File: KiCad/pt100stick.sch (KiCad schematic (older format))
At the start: 9 parts, among them U1 MAX31865ATP_

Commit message: Start Project Lib / Relayout
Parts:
- A1: symbol Driver_Motor:Pololu_Breakout_A4988 -> PT100stick:Pololu_Breakout_A4988
- C1, C2: symbol Device:C_Small -> PT100stick:C_Small
- FB1: symbol Device:Ferrite_Bead_Small -> PT100stick:Ferrite_Bead_Small
- JP1, JP2: footprint Jumper:SolderJumper-2_P1.3mm_Open_TrianglePad1.0x1.5mm -> Jumper:SolderJumper-2_P1.3mm_Bridged_Pad1.0x1.5mm; symbol Jumper:SolderJumper_2_Bridged -> PT100stick:SolderJumper_2_Bridged
- R1: symbol Device:R_Small_US -> PT100stick:R_Small_US
- U1: symbol dk_PMIC-Thermal-Management:MAX31865ATP_ -> PT100stick:MAX31865ATP_
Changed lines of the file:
@@
 $EndDescr
 $Comp
-L Driver_Motor:Pololu_Breakout_A4988 A1
+L PT100stick:Pololu_Breakout_A4988 A1
 U 1 1 5EB9E565
 P 1900 2050
@@
 SCK
 $Comp
-L power:GND #PWR0101
+L PT100stick:GND #PWR0101
 U 1 1 5EBA0B0B
 P 2000 2950
@@
 	2000 2900 2100 2900
 $Comp
-L power:+3.3V #PWR0102
+L PT100stick:+3.3V #PWR0102
 U 1 1 5EBA1652
 P 1900 1100
@@
 	1900 1100 1900 1350
 $Comp
-L dk_PMIC-Thermal-Management:MAX31865ATP_ U1
+L PT100stick:MAX31865ATP_ U1
 U 1 1 5EBA27E8
 P 5150 1700
@@
 	4450 2500 4650 2500
 $Comp
-L power:GND #PWR0104
+L PT100stick:GND #PWR0104
 U 1 1 5EBA5AB3
 P 5200 2900
@@
 Wire Wire Line
 	5200 2850 5250 2850
-$Comp
-L power:+3.3V #PWR0105
-U 1 1 5EBA7D45
-P 5200 900
-F 0 "#PWR0105" H 5200 750 50  0001 C CNN
-F 1 "+3.3V" H 5215 1073 50  0000 C CNN
-F 2 "" H 5200 900 50  0001 C CNN
-F 3 "" H 5200 900 50  0001 C CNN
-	1    5200 900
-	1    0    0    -1
-$EndComp
 Wire Wire Line
 	5200 900  5200 950
@@
 	4600 1800 4650 1800
 $Comp
-L Device:R_Small_US R1
+L PT100stick:R_Small_US R1
 U 1 1 5EBADD3B
 P 4250 1700
@@
 FORCE+
 $Comp
-L Device:C_Small C1
+L PT100stick:C_Small C1
 U 1 1 5EBB292B
 P 2950 2100
@@
 $EndComp
 $Comp
-L Jumper:SolderJumper_2_Bridged JP1
+L PT100stick:SolderJumper_2_Bridged JP1
 U 1 1 5EBAE765
 P 2650 2250
 F 0 "JP1" H 2650 2025 50  0000 C CNN
 F 1 "Cut for 4" H 2650 2116 50  0000 C CNN
-F 2 "Jumper:SolderJumper-2_P1.3mm_Open_TrianglePad1.0x1.5mm" H 2650 2250 50  0001 C CNN
+F 2 "Jumper:SolderJumper-2_P1.3mm_Bridged_Pad1.0x1.5mm" H 2650 2250 50  0001 C CNN
 F 3 "~" H 2650 2250 50  0001 C CNN
 	1    2650 2250
@@
 $EndComp
 $Comp
-L Jumper:SolderJumper_2_Bridged JP2
+L PT100stick:SolderJumper_2_Bridged JP2
 U 1 1 5EBB06B7
 P 2650 1950
 F 0 "JP2" H 2650 2155 50  0000 C CNN
 F 1 "Cut for 3/4" H 2650 2064 50  0000 C CNN
-F 2 "Jumper:SolderJumper-2_P1.3mm_Open_TrianglePad1.0x1.5mm" H 2650 1950 50  0001 C CNN
+F 2 "Jumper:SolderJumper-2_P1.3mm_Bridged_Pad1.0x1.5mm" H 2650 1950 50  0001 C CNN
 F 3 "~" H 2650 1950 50  0001 C CNN
 	1    2650 1950
@@
 FORCE-
 $Comp
-L Device:C_Small C2
+L PT100stick:C_Small C2
 U 1 1 5EC2A459
-P 6000 1050
-F 0 "C2" H 6092 1096 50  0000 L CNN
-F 1 "0.1uF" H 6092 1005 50  0000 L CNN
-F 2 "Capacitor_SMD:C_0603_1608Metric_Pad1.05x0.95mm_HandSolder" H 6000 1050 50  0001 C CNN
-F 3 "~" H 6000 1050 50  0001 C CNN
-	1    6000 1050
-	1    0    0    -1
-$EndComp
-$Comp
-L power:+3.3V #PWR0103
-U 1 1 5EC2B8B9
-P 6000 900
-F 0 "#PWR0103" H 6000 750 50  0001 C CNN
-F 1 "+3.3V" H 6015 1073 50  0000 C CNN
-F 2 "" H 6000 900 50  0001 C CNN
-F 3 "" H 6000 900 50  0001 C CNN
-	1    6000 900
-	1    0    0    -1
-$EndComp
-Wire Wire Line
-	6000 900  6000 950
-$Comp
-L power:GND #PWR0107
-U 1 1 5EC2E090
-P 6000 1200
-F 0 "#PWR0107" H 6000 950 50  0001 C CNN
-F 1 "GND" H 6005 1027 50  0000 C CNN
-F 2 "" H 6000 1200 50  0001 C CNN
-F 3 "" H 6000 1200 50  0001 C CNN
-	1    6000 1200
-	1    0    0    -1
-$EndComp
-Wire Wire Line
-	6000 1150 6000 1200
-$Comp
-L Device:Ferrite_Bead_Small FB1
+P 6250 1650
+F 0 "C2" H 6342 1696 50  0000 L CNN
+F 1 "0.1uF" H 6342 1605 50  0000 L CNN
+F 2 "Capacitor_SMD:C_0603_1608Metric_Pad1.05x0.95mm_HandSolder" H 6250 1650 50  0001 C CNN
+F 3 "~" H 6250 1650 50  0001 C CNN
+	1    6250 1650
+	1    0    0    -1
+$EndComp
+Wire Wire Line
+	6250 1500 6250 1550
+Wire Wire Line
+	6250 1750 6250 1800
+$Comp
+L PT100stick:Ferrite_Bead_Small FB1
 U 1 1 5EC32E91
 P 5250 1150
@@
 Wire Wire Line
 	5250 1400 5250 1250
+$Comp
+L PT100stick:+3.3V #PWR?
+U 1 1 5EBCE55F
+P 5200 900
+F 0 "#PWR?" H 5200 750 50  0001 C CNN
+F 1 "+3.3V" H 5215 1073 50  0000 C CNN
+F 2 "" H 5200 900 50  0001 C CNN
+F 3 "" H 5200 900 50  0001 C CNN
+	1    5200 900
+	1    0    0    -1
+$EndComp
+$Comp
+L PT100stick:+3.3V #PWR?
+U 1 1 5EBD5DBE
+P 6250 1500
+F 0 "#PWR?" H 6250 1350 50  0001 C CNN
+F 1 "+3.3V" H 6265 1673 50  0000 C CNN
+F 2 "" H 6250 1500 50  0001 C CNN
+F 3 "" H 6250 1500 50  0001 C CNN
+	1    6250 1500
+	1    0    0    -1
+$EndComp
+$Comp
+L PT100stick:GND #PWR?
+U 1 1 5EBD76AE
+P 6250 1800
+F 0 "#PWR?" H 6250 1550 50  0001 C CNN
+F 1 "GND" H 6255 1627 50  0000 C CNN
+F 2 "" H 6250 1800 50  0001 C CNN
+F 3 "" H 6250 1800 50  0001 C CNN
+	1    6250 1800
+	1    0    0    -1
+$EndComp
 $EndSCHEMATC

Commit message: Moved all footprints to project lib (I think)
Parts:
- A1: footprint Module:Pololu_Breakout-16_15.2x20.3mm -> PT100Stick:Pololu_Breakout-16_15.2x20.3mm
- C1, C2: footprint Capacitor_SMD:C_0603_1608Metric_Pad1.05x0.95mm_HandSolder -> PT100Stick:C_0603_1608Metric_Pad1.05x0.95mm_HandSolder
- FB1: footprint Inductor_SMD:L_0603_1608Metric_Pad1.05x0.95mm_HandSolder -> PT100Stick:L_0603_1608Metric_Pad1.05x0.95mm_HandSolder
- JP1, JP2: footprint Jumper:SolderJumper-2_P1.3mm_Bridged_Pad1.0x1.5mm -> PT100Stick:SolderJumper-2_P1.3mm_Bridged_Pad1.0x1.5mm
- JP3: footprint Jumper:SolderJumper-3_P1.3mm_Bridged12_Pad1.0x1.5mm -> PT100Stick:SolderJumper-3_P1.3mm_Bridged12_Pad1.0x1.5mm
- R1: footprint Resistor_SMD:R_0603_1608Metric_Pad1.05x0.95mm_HandSolder -> PT100Stick:R_0603_1608Metric_Pad1.05x0.95mm_HandSolder
- U1: footprint digikey-footprints:TQFN-20-1EP_5x5mm -> PT100Stick:TQFN-20-1EP_5x5mm_P0.65mm_EP3.1x3.1mm
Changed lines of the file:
@@
 F 0 "A1" H 1950 2931 50  0000 C CNN
 F 1 "Pololu_Breakout_A4988" H 1950 2840 50  0000 C CNN
-F 2 "Module:Pololu_Breakout-16_15.2x20.3mm" H 2175 1300 50  0001 L CNN
+F 2 "PT100Stick:Pololu_Breakout-16_15.2x20.3mm" H 2175 1300 50  0001 L CNN
 F 3 "https://www.pololu.com/product/2980/pictures" H 2000 1750 50  0001 C CNN
 	1    1900 2050
@@
 F 0 "U1" H 4800 2200 60  0000 C CNN
 F 1 "MAX31865ATP_" H 4800 2100 60  0000 C CNN
-F 2 "digikey-footprints:TQFN-20-1EP_5x5mm" H 5350 1900 60  0001 L CNN
+F 2 "PT100Stick:TQFN-20-1EP_5x5mm_P0.65mm_EP3.1x3.1mm" H 5350 1900 60  0001 L CNN
 F 3 "https://datasheets.maximintegrated.com/en/ds/MAX31865.pdf" H 5350 2000 60  0001 L CNN
 F 4 "MAX31865ATP+-ND" H 5350 2100 60  0001 L CNN "Digi-Key_PN"
@@
 F 0 "R1" H 4183 1654 50  0000 R CNN
 F 1 "430" H 4183 1745 50  0000 R CNN
-F 2 "Resistor_SMD:R_0603_1608Metric_Pad1.05x0.95mm_HandSolder" H 4250 1700 50  0001 C CNN
+F 2 "PT100Stick:R_0603_1608Metric_Pad1.05x0.95mm_HandSolder" H 4250 1700 50  0001 C CNN
 F 3 "~" H 4250 1700 50  0001 C CNN
 	1    4250 1700
@@
 F 0 "C1" H 3042 2146 50  0000 L CNN
 F 1 "0.1uF" H 3042 2055 50  0000 L CNN
-F 2 "Capacitor_SMD:C_0603_1608Metric_Pad1.05x0.95mm_HandSolder" H 2950 2100 50  0001 C CNN
+F 2 "PT100Stick:C_0603_1608Metric_Pad1.05x0.95mm_HandSolder" H 2950 2100 50  0001 C CNN
 F 3 "~" H 2950 2100 50  0001 C CNN
 	1    2950 2100
@@
 F 0 "JP1" H 2650 2025 50  0000 C CNN
 F 1 "Cut for 4" H 2650 2116 50  0000 C CNN
-F 2 "Jumper:SolderJumper-2_P1.3mm_Bridged_Pad1.0x1.5mm" H 2650 2250 50  0001 C CNN
+F 2 "PT100Stick:SolderJumper-2_P1.3mm_Bridged_Pad1.0x1.5mm" H 2650 2250 50  0001 C CNN
 F 3 "~" H 2650 2250 50  0001 C CNN
 	1    2650 2250
@@
 F 0 "JP2" H 2650 2155 50  0000 C CNN
 F 1 "Cut for 3/4" H 2650 2064 50  0000 C CNN
-F 2 "Jumper:SolderJumper-2_P1.3mm_Bridged_Pad1.0x1.5mm" H 2650 1950 50  0001 C CNN
+F 2 "PT100Stick:SolderJumper-2_P1.3mm_Bridged_Pad1.0x1.5mm" H 2650 1950 50  0001 C CNN
 F 3 "~" H 2650 1950 50  0001 C CNN
 	1    2650 1950
@@
 F 0 "JP3" V 3300 1950 50  0000 L CNN
 F 1 "SolderJumper_3_Bridged12" V 2750 1700 50  0000 L CNN
-F 2 "Jumper:SolderJumper-3_P1.3mm_Bridged12_Pad1.0x1.5mm" H 3400 2200 50  0001 C CNN
+F 2 "PT100Stick:SolderJumper-3_P1.3mm_Bridged12_Pad1.0x1.5mm" H 3400 2200 50  0001 C CNN
 F 3 "~" H 3400 2200 50  0001 C CNN
 	1    3400 2200
@@
 F 0 "C2" H 6342 1696 50  0000 L CNN
 F 1 "0.1uF" H 6342 1605 50  0000 L CNN
-F 2 "Capacitor_SMD:C_0603_1608Metric_Pad1.05x0.95mm_HandSolder" H 6250 1650 50  0001 C CNN
+F 2 "PT100Stick:C_0603_1608Metric_Pad1.05x0.95mm_HandSolder" H 6250 1650 50  0001 C CNN
 F 3 "~" H 6250 1650 50  0001 C CNN
 	1    6250 1650
@@
 F 0 "FB1" H 5350 1196 50  0000 L CNN
 F 1 "Ferrite_Bead_Small" H 5350 1105 50  0000 L CNN
-F 2 "Inductor_SMD:L_0603_1608Metric_Pad1.05x0.95mm_HandSolder" V 5180 1150 50  0001 C CNN
+F 2 "PT100Stick:L_0603_1608Metric_Pad1.05x0.95mm_HandSolder" V 5180 1150 50  0001 C CNN
 F 3 "~" H 5250 1150 50  0001 C CNN
 	1    5250 1150
@@
 	5250 1400 5250 1250
 $Comp
-L PT100stick:+3.3V #PWR?
+L PT100stick:+3.3V #PWR0103
 U 1 1 5EBCE55F
 P 5200 900
-F 0 "#PWR?" H 5200 750 50  0001 C CNN
+F 0 "#PWR0103" H 5200 750 50  0001 C CNN
 F 1 "+3.3V" H 5215 1073 50  0000 C CNN
 F 2 "" H 5200 900 50  0001 C CNN
@@
 $EndComp
 $Comp
-L PT100stick:+3.3V #PWR?
+L PT100stick:+3.3V #PWR0105
 U 1 1 5EBD5DBE
 P 6250 1500
-F 0 "#PWR?" H 6250 1350 50  0001 C CNN
+F 0 "#PWR0105" H 6250 1350 50  0001 C CNN
 F 1 "+3.3V" H 6265 1673 50  0000 C CNN
 F 2 "" H 6250 1500 50  0001 C CNN
@@
 $EndComp
 $Comp
-L PT100stick:GND #PWR?
+L PT100stick:GND #PWR0107
 U 1 1 5EBD76AE
 P 6250 1800
-F 0 "#PWR?" H 6250 1550 50  0001 C CNN
+F 0 "#PWR0107" H 6250 1550 50  0001 C CNN
 F 1 "GND" H 6255 1627 50  0000 C CNN
 F 2 "" H 6250 1800 50  0001 C CNN

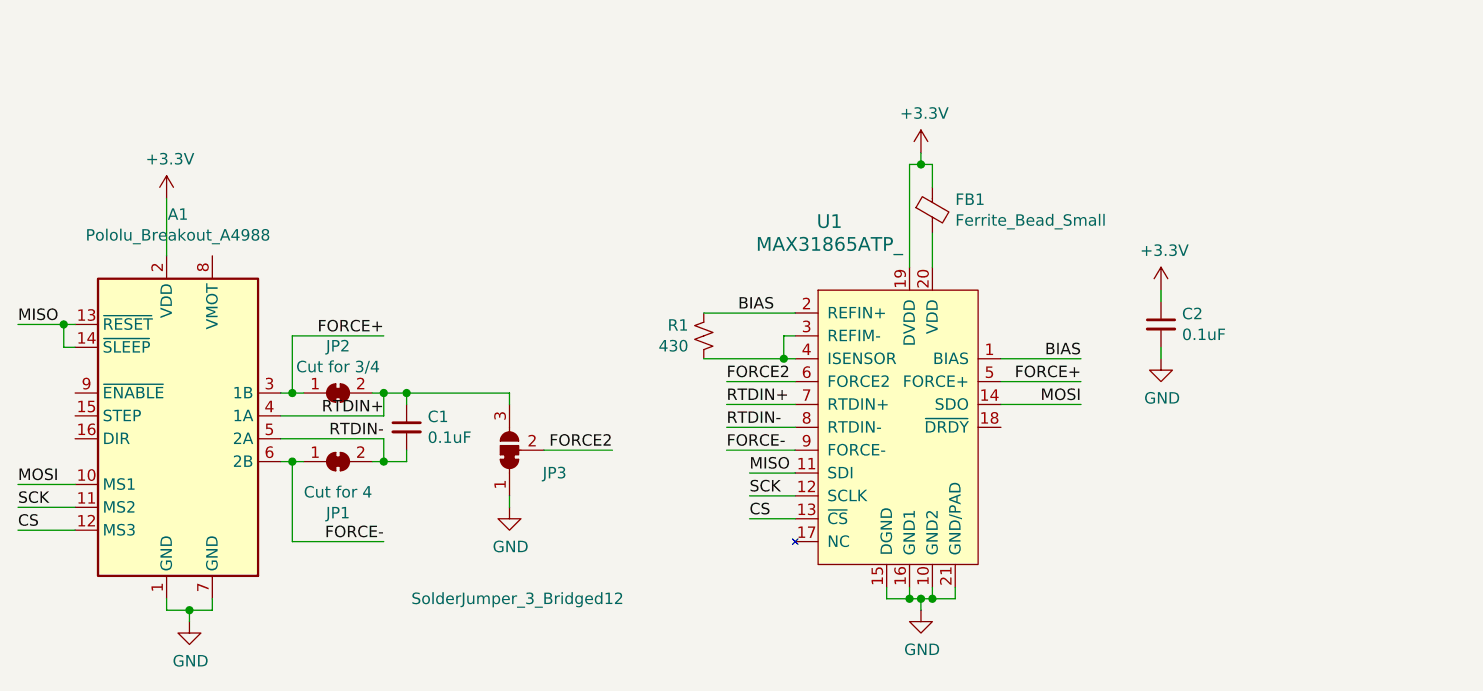
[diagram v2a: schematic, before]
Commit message: Reworked layout
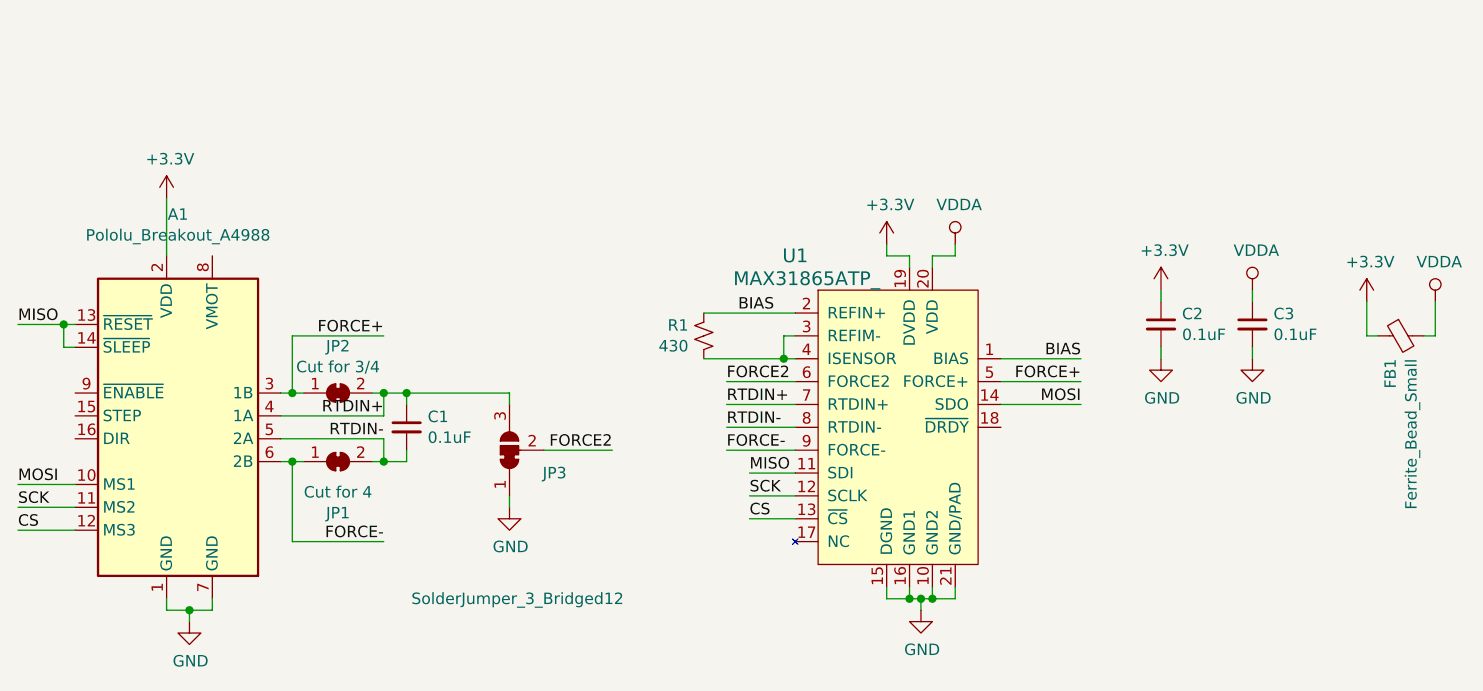
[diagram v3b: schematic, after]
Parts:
- added C3: 0.1uF, PT100Stick:C_0603_1608Metric_Pad1.05x0.95mm_HandSolder, symbol PT100stick:C_Small
- JP1, JP2: footprint PT100Stick:SolderJumper-2_P1.3mm_Bridged_Pad1.0x1.5mm -> PT100Stick:SolderJumper-2_P1.3mm_Bridged_RoundedPad1.0x1.5mm
- JP3: footprint PT100Stick:SolderJumper-3_P1.3mm_Bridged12_Pad1.0x1.5mm -> PT100Stick:SolderJumper-3_P1.3mm_Bridged12_RoundedPad1.0x1.5mm
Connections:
- net GND: now also C3.2
- net VDDA: now reaches FB1.2, U1.20 (VDD)
- net VDDA: now also C3.1
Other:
- moved on the sheet: FB1
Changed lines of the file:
@@
 U 1 1 5EBA27E8
 P 5150 1700
-F 0 "U1" H 4800 2200 60  0000 C CNN
-F 1 "MAX31865ATP_" H 4800 2100 60  0000 C CNN
+F 0 "U1" H 4650 2050 60  0000 C CNN
+F 1 "MAX31865ATP_" H 4700 1950 60  0000 C CNN
 F 2 "PT100Stick:TQFN-20-1EP_5x5mm_P0.65mm_EP3.1x3.1mm" H 5350 1900 60  0001 L CNN
 F 3 "https://datasheets.maximintegrated.com/en/ds/MAX31865.pdf" H 5350 2000 60  0001 L CNN
@@
 Wire Wire Line
 	5200 2850 5250 2850
-Wire Wire Line
-	5200 900  5200 950
-Wire Wire Line
-	5200 950  5150 950
-Wire Wire Line
-	5150 950  5150 1400
 $Comp
 L power:GND #PWR0106
@@
 F 0 "JP1" H 2650 2025 50  0000 C CNN
 F 1 "Cut for 4" H 2650 2116 50  0000 C CNN
-F 2 "PT100Stick:SolderJumper-2_P1.3mm_Bridged_Pad1.0x1.5mm" H 2650 2250 50  0001 C CNN
+F 2 "PT100Stick:SolderJumper-2_P1.3mm_Bridged_RoundedPad1.0x1.5mm" H 2650 2250 50  0001 C CNN
 F 3 "~" H 2650 2250 50  0001 C CNN
 	1    2650 2250
@@
 F 0 "JP2" H 2650 2155 50  0000 C CNN
 F 1 "Cut for 3/4" H 2650 2064 50  0000 C CNN
-F 2 "PT100Stick:SolderJumper-2_P1.3mm_Bridged_Pad1.0x1.5mm" H 2650 1950 50  0001 C CNN
+F 2 "PT100Stick:SolderJumper-2_P1.3mm_Bridged_RoundedPad1.0x1.5mm" H 2650 1950 50  0001 C CNN
 F 3 "~" H 2650 1950 50  0001 C CNN
 	1    2650 1950
@@
 F 0 "JP3" V 3300 1950 50  0000 L CNN
 F 1 "SolderJumper_3_Bridged12" V 2750 1700 50  0000 L CNN
-F 2 "PT100Stick:SolderJumper-3_P1.3mm_Bridged12_Pad1.0x1.5mm" H 3400 2200 50  0001 C CNN
+F 2 "PT100Stick:SolderJumper-3_P1.3mm_Bridged12_RoundedPad1.0x1.5mm" H 3400 2200 50  0001 C CNN
 F 3 "~" H 3400 2200 50  0001 C CNN
 	1    3400 2200
@@
 L PT100stick:Ferrite_Bead_Small FB1
 U 1 1 5EC32E91
-P 5250 1150
-F 0 "FB1" H 5350 1196 50  0000 L CNN
-F 1 "Ferrite_Bead_Small" H 5350 1105 50  0000 L CNN
-F 2 "PT100Stick:L_0603_1608Metric_Pad1.05x0.95mm_HandSolder" V 5180 1150 50  0001 C CNN
-F 3 "~" H 5250 1150 50  0001 C CNN
-	1    5250 1150
-	1    0    0    -1
-$EndComp
-Wire Wire Line
-	5250 1050 5250 950
-Wire Wire Line
-	5250 950  5200 950
-Connection ~ 5200 950
-Wire Wire Line
-	5250 1400 5250 1250
+P 7300 1700
+F 0 "FB1" H 7400 1746 50  0000 L CNN
+F 1 "Ferrite_Bead_Small" H 7400 1655 50  0000 L CNN
+F 2 "PT100Stick:L_0603_1608Metric_Pad1.05x0.95mm_HandSolder" V 7230 1700 50  0001 C CNN
+F 3 "~" H 7300 1700 50  0001 C CNN
+	1    7300 1700
+	0    -1   1    0
+$EndComp
 $Comp
 L PT100stick:+3.3V #PWR0103
 U 1 1 5EBCE55F
-P 5200 900
-F 0 "#PWR0103" H 5200 750 50  0001 C CNN
-F 1 "+3.3V" H 5215 1073 50  0000 C CNN
-F 2 "" H 5200 900 50  0001 C CNN
-F 3 "" H 5200 900 50  0001 C CNN
-	1    5200 900
+P 7150 1550
+F 0 "#PWR0103" H 7150 1400 50  0001 C CNN
+F 1 "+3.3V" H 7165 1723 50  0000 C CNN
+F 2 "" H 7150 1550 50  0001 C CNN
+F 3 "" H 7150 1550 50  0001 C CNN
+	1    7150 1550
 	1    0    0    -1
 $EndComp
@@
 	1    0    0    -1
 $EndComp
+Wire Wire Line
+	7150 1700 7200 1700
+$Comp
+L power:VDDA #PWR0108
+U 1 1 5EBDF6C7
+P 7450 1550
+F 0 "#PWR0108" H 7450 1400 50  0001 C CNN
+F 1 "VDDA" H 7467 1723 50  0000 C CNN
+F 2 "" H 7450 1550 50  0001 C CNN
+F 3 "" H 7450 1550 50  0001 C CNN
+	1    7450 1550
+	1    0    0    -1
+$EndComp
+Wire Wire Line
+	7450 1550 7450 1700
+Wire Wire Line
+	7450 1700 7400 1700
+Wire Wire Line
+	7150 1550 7150 1700
+$Comp
+L PT100stick:+3.3V #PWR0109
+U 1 1 5EBE7038
+P 5050 1300
+F 0 "#PWR0109" H 5050 1150 50  0001 C CNN
+F 1 "+3.3V" H 5065 1473 50  0000 C CNN
+F 2 "" H 5050 1300 50  0001 C CNN
+F 3 "" H 5050 1300 50  0001 C CNN
+	1    5050 1300
+	1    0    0    -1
+$EndComp
+$Comp
+L power:VDDA #PWR0110
+U 1 1 5EBE703E
+P 5350 1300
+F 0 "#PWR0110" H 5350 1150 50  0001 C CNN
+F 1 "VDDA" H 5367 1473 50  0000 C CNN
+F 2 "" H 5350 1300 50  0001 C CNN
+F 3 "" H 5350 1300 50  0001 C CNN
+	1    5350 1300
+	1    0    0    -1
+$EndComp
+Wire Wire Line
+	5050 1300 5050 1350
+Wire Wire Line
+	5050 1350 5150 1350
+Wire Wire Line
+	5150 1350 5150 1400
+Wire Wire Line
+	5250 1400 5250 1350
+Wire Wire Line
+	5350 1350 5350 1300
+Wire Wire Line
+	5250 1350 5350 1350
+$Comp
+L PT100stick:C_Small C3
+U 1 1 5EBF6A4F
+P 6650 1650
+F 0 "C3" H 6742 1696 50  0000 L CNN
+F 1 "0.1uF" H 6742 1605 50  0000 L CNN
+F 2 "PT100Stick:C_0603_1608Metric_Pad1.05x0.95mm_HandSolder" H 6650 1650 50  0001 C CNN
+F 3 "~" H 6650 1650 50  0001 C CNN
+	1    6650 1650
+	1    0    0    -1
+$EndComp
+Wire Wire Line
+	6650 1500 6650 1550
+Wire Wire Line
+	6650 1750 6650 1800
+$Comp
+L PT100stick:GND #PWR0111
+U 1 1 5EBF6A5D
+P 6650 1800
+F 0 "#PWR0111" H 6650 1550 50  0001 C CNN
+F 1 "GND" H 6655 1627 50  0000 C CNN
+F 2 "" H 6650 1800 50  0001 C CNN
+F 3 "" H 6650 1800 50  0001 C CNN
+	1    6650 1800
+	1    0    0    -1
+$EndComp
+$Comp
+L power:VDDA #PWR0112
+U 1 1 5EBF8573
+P 6650 1500
+F 0 "#PWR0112" H 6650 1350 50  0001 C CNN
+F 1 "VDDA" H 6667 1673 50  0000 C CNN
+F 2 "" H 6650 1500 50  0001 C CNN
+F 3 "" H 6650 1500 50  0001 C CNN
+	1    6650 1500
+	1    0    0    -1
+$EndComp

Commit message: Hopefully stable release :D
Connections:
- net MISO: now also A1.10 (MS1); no longer A1.13 (~RESET), A1.14 (~SLEEP)
- net MOSI: now also A1.13 (~RESET), A1.14 (~SLEEP); no longer A1.10 (MS1)
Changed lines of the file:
@@
 Wire Wire Line
 	1500 2350 1250 2350
+Text Label 1250 1650 0    50   ~ 0
+MOSI
 Text Label 1250 2350 0    50   ~ 0
-MOSI
-Text Label 1250 1650 0    50   ~ 0
 MISO
 Text Label 1250 2550 0    50   ~ 0

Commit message: Quick fixes
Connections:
- net GND: no longer A1.1 (GND)
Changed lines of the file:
@@
 Comment4 ""
 $EndDescr
-$Comp
-L PT100stick:Pololu_Breakout_A4988 A1
-U 1 1 5EB9E565
-P 1900 2050
-F 0 "A1" H 1950 2931 50  0000 C CNN
-F 1 "Pololu_Breakout_A4988" H 1950 2840 50  0000 C CNN
-F 2 "PT100Stick:Pololu_Breakout-16_15.2x20.3mm" H 2175 1300 50  0001 L CNN
-F 3 "https://www.pololu.com/product/2980/pictures" H 2000 1750 50  0001 C CNN
-	1    1900 2050
-	1    0    0    -1
-$EndComp
 Wire Wire Line
 	1500 2550 1250 2550
@@
 L PT100stick:GND #PWR0101
 U 1 1 5EBA0B0B
-P 2000 2950
-F 0 "#PWR0101" H 2000 2700 50  0001 C CNN
-F 1 "GND" H 2005 2777 50  0000 C CNN
-F 2 "" H 2000 2950 50  0001 C CNN
-F 3 "" H 2000 2950 50  0001 C CNN
-	1    2000 2950
-	1    0    0    -1
-$EndComp
-Wire Wire Line
-	1900 2850 1900 2900
-Wire Wire Line
-	2100 2900 2100 2850
-Wire Wire Line
-	1900 2900 2000 2900
-Wire Wire Line
-	2000 2950 2000 2900
-Connection ~ 2000 2900
-Wire Wire Line
-	2000 2900 2100 2900
+P 2100 2950
+F 0 "#PWR0101" H 2100 2700 50  0001 C CNN
+F 1 "GND" H 2105 2777 50  0000 C CNN
+F 2 "" H 2100 2950 50  0001 C CNN
+F 3 "" H 2100 2950 50  0001 C CNN
+	1    2100 2950
+	1    0    0    -1
+$EndComp
 $Comp
 L PT100stick:+3.3V #PWR0102
@@
 	1    0    0    -1
 $EndComp
+$Comp
+L PT100stick:Pololu_Breakout_A4988 A1
+U 1 1 5EB9E565
+P 1900 2050
+F 0 "A1" H 1950 2931 50  0000 C CNN
+F 1 "Pololu_Breakout_A4988" H 1950 2840 50  0000 C CNN
+F 2 "PT100Stick:Pololu_Breakout-16_15.2x20.3mm" H 2175 1300 50  0001 L CNN
+F 3 "https://www.pololu.com/product/2980/pictures" H 2000 1750 50  0001 C CNN
+	1    1900 2050
+	1    0    0    -1
+$EndComp
+Wire Wire Line
+	2100 2850 2100 2950
 $EndSCHEMATC
